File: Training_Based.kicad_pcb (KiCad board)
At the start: 2 copper layers, 210 x 140 mm, 6 parts

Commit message: update
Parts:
- added K1: FINDER-36.11, Relay_THT:Relay_SPDT_Finder_36.11, F.Cu at (191.1, 94.7)
- added K2: FINDER-36.11, Relay_THT:Relay_SPDT_Finder_36.11, F.Cu at (191.2, 76.5)
- added REF**: 7SegmentLED_LTS6760_LTS6780, Display_7Segment:7SegmentLED_LTS6760_LTS6780, F.Cu at (187.1, 45.2)
- added REF**: TerminalBlock_Altech_AK300-4_P5.00mm, TerminalBlock:TerminalBlock_Altech_AK300-4_P5.00mm, F.Cu at (218.2, 75.7)
- added REF**: 7SegmentLED_LTS6760_LTS6780, Display_7Segment:7SegmentLED_LTS6760_LTS6780, F.Cu at (200.5, 45.1)
- added REF**: ESP32-DOIT-DEVKIT, doit-esp32-devkit-kicad:ESP32-DOIT-DEVKIT, F.Cu at (126.3, 102.3)
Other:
- board text added: "ANALOG INPUT"
- board text added: "BUZZER"
- board text added: "ESP32"
- board text added: "LED OUTPUT"
- board text added: "OPTO INPUT"
- board text added: "PIR SENSOR"
- board text added: "POWER SUPPLY"
- board text added: "PROTOBOARD"
- board text added: "RELAY OUTPUT"
- board text added: "SERIAL BUS BREAKOUT AREA"
- board text added: "TEMP/HUMID"
- board text added: "ULTRASONIC SENSOR"
- board text added: "VOLUME LDR"

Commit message: update
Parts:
- removed REF** (x2): 7SegmentLED_LTS6760_LTS6780, Display_7Segment:7SegmentLED_LTS6760_LTS6780
- removed REF**: TerminalBlock_Altech_AK300-4_P5.00mm, TerminalBlock:TerminalBlock_Altech_AK300-4_P5.00mm
- removed REF**: ESP32-DOIT-DEVKIT, doit-esp32-devkit-kicad:ESP32-DOIT-DEVKIT
- added AFF1: LTS-6980HR, Display_7Segment:7SegmentLED_LTS6760_LTS6780, F.Cu at (188.2, 41.6)
- added AFF2: LTS-6980HR, Display_7Segment:7SegmentLED_LTS6760_LTS6780, F.Cu at (202.1, 41.6)
- added BZ1: Buzzer, Buzzer_Beeper:Buzzer_12x9.5RM7.6, F.Cu at (115.0, 34.6)
- added U1: HC-SR04, Library:HC-SR04, F.Cu at (63.9, 33.2)
- added U2: DHT11, Sensor:Aosong_DHT11_5.5x12.0_P2.54mm, F.Cu at (50.6, 29.6)
- moved K1 9.49 mm to (182.8, 90.0)
- moved K2 9.49 mm to (182.9, 71.8)
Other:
- board text added: "7SEGMENT LED"

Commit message: add spacerx6
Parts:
- added U3: Protoboard, Library:Protoboard, F.Cu at (126.0, 73.3)
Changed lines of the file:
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@@
     (pad "1" thru_hole circle (at 2.4 0) (size 0.8 0.8) (drill 0.5) (layers *.Cu *.Mask)
       (net 1 "GND") (pinfunction "1") (pintype "input"))
+    (model "${KIPRJMOD}/3D Model/Plastic Stick Fixed Clip On PCB.stp"
+      (offset (xyz 0 0 -14))
+      (scale (xyz 1 1 1))
+      (rotate (xyz 0 0 0))
+    )
   )
   (footprint "Relay_THT:Relay_SPDT_Finder_36.11" (layer "F.Cu")
@@
     (pad "1" thru_hole circle (at 2.4 0) (size 0.8 0.8) (drill 0.5) (layers *.Cu *.Mask)
       (net 1 "GND") (pinfunction "1") (pintype "input"))
+    (model "${KIPRJMOD}/3D Model/Plastic Stick Fixed Clip On PCB.stp"
+      (offset (xyz 0 0 -14))
+      (scale (xyz 1 1 1))
+      (rotate (xyz 0 0 0))
+    )
   )
   (footprint "MountingHole:MountingHole_3.2mm_M3_Pad_Via" (layer "F.Cu")
@@
     (pad "1" thru_hole circle (at 2.4 0) (size 0.8 0.8) (drill 0.5) (layers *.Cu *.Mask)
       (net 1 "GND") (pinfunction "1") (pintype "input"))
+    (model "${KIPRJMOD}/3D Model/Plastic Stick Fixed Clip On PCB.stp"
+      (offset (xyz 0 0 -14))
+      (scale (xyz 1 1 1))
+      (rotate (xyz 0 0 0))
+    )
   )
   (footprint "MountingHole:MountingHole_3.2mm_M3_Pad_Via" (layer "F.Cu")
@@
     (pad "1" thru_hole circle (at 2.4 0) (size 0.8 0.8) (drill 0.5) (layers *.Cu *.Mask)
       (net 1 "GND") (pinfunction "1") (pintype "input"))
+    (model "${KIPRJMOD}/3D Model/Plastic Stick Fixed Clip On PCB.stp"
+      (offset (xyz 0 0 -14))
+      (scale (xyz 1 1 1))
+      (rotate (xyz 0 0 0))
+    )
   )
   (footprint "Buzzer_Beeper:Buzzer_12x9.5RM7.6" (layer "F.Cu")
@@
     )
   )
+  (footprint "Library:Protoboard" (layer "F.Cu")
+    (at 125.95 73.3)
+    (property "Sheetfile" "Training_Based.kicad_sch")
+    (property "Sheetname" "")
+    (attr smd)
+    (fp_text reference "U3" (at 0 -0.5 unlocked) (layer "F.SilkS")
+        (effects (font (size 1 1) (thickness 0.15)))
+    )
+    (fp_text value "Protoboard" (at 0 1 unlocked) (layer "F.Fab")
+        (effects (font (size 1 1) (thickness 0.15)))
+    )
+    (fp_text user "${REFERENCE}" (at 0 2.5 unlocked) (layer "F.Fab")
+        (effects (font (size 1 1) (thickness 0.15)))
+    )
+    (fp_rect (start -41 -27) (end 41 27)
+      (stroke (width 0.12) (type default)) (fill none) (layer "F.SilkS"))
+    (model "${KIPRJMOD}/3D Model/proto_400.step"
+      (offset (xyz 0 0 0))
+      (scale (xyz 1 1 1))
+      (rotate (xyz 0 0 90))
+    )
+  )
   (footprint "Relay_THT:Relay_SPDT_Finder_36.11" (layer "F.Cu")
     (at 182.8 89.95)
@@
     (pad "1" thru_hole circle (at 2.4 0) (size 0.8 0.8) (drill 0.5) (layers *.Cu *.Mask)
       (net 1 "GND") (pinfunction "1") (pintype "input"))
+    (model "${KIPRJMOD}/3D Model/Plastic Stick Fixed Clip On PCB.stp"
+      (offset (xyz 0 0 -14))
+      (scale (xyz 1 1 1))
+      (rotate (xyz 0 0 0))
+    )
   )
   (footprint "MountingHole:MountingHole_3.2mm_M3_Pad_Via" (layer "F.Cu")
@@
     (pad "1" thru_hole circle (at 2.4 0) (size 0.8 0.8) (drill 0.5) (layers *.Cu *.Mask)
       (net 1 "GND") (pinfunction "1") (pintype "input"))
-  )
-  (gr_rect (start 226.025 113.5) (end 165.125 151.9)
+    (model "${KIPRJMOD}/3D Model/Plastic Stick Fixed Clip On PCB.stp"
+      (offset (xyz 0 0 -14))
+      (scale (xyz 1 1 1))
+      (rotate (xyz 0 0 0))
+    )
+  )
+  (gr_rect (start 175.7996 113.5) (end 226.025 151.9)
     (stroke (width 0.1) (type default)) (fill none) (layer "F.SilkS"))
   (gr_rect (start 182.95 24.025) (end 224.5 44.05)
@@
   (gr_rect (start 109.7 23.975) (end 134 44)
     (stroke (width 0.1) (type default)) (fill none) (layer "F.SilkS"))
-  (gr_rect (start 96.8 104) (end 152.05 152.3)
+  (gr_rect (start 125.15 104) (end 169.95 152.3)
     (stroke (width 0.1) (type default)) (fill none) (layer "F.SilkS"))
   (gr_rect (start 23.975 124.95) (end 71.125 151.55)
@@
     (effects (font (size 2.54 2.54) (thickness 0.2)) (justify bottom))
   )
-  (gr_text "ESP32" (at 118.481381 129.57) (layer "F.SilkS")
+  (gr_text "ESP32" (at 143.55 128.75) (layer "F.SilkS")
     (effects (font (size 2.54 2.54) (thickness 0.2) bold) (justify left bottom))
   )

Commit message: ีWork in Progress
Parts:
- removed H5, H6: MountingHole_Pad, MountingHole:MountingHole_3.2mm_M3_Pad_Via
- removed U3: Protoboard, Library:Protoboard
- added J1: Conn_01x19, Connector_PinHeader_2.54mm:PinHeader_1x19_P2.54mm_Vertical, F.Cu at (110.8, 107.2)
- added J2: Conn_01x19, Connector_PinSocket_2.54mm:PinSocket_1x19_P2.54mm_Vertical, F.Cu at (114.5, 107.2)
- added J3: Conn_01x19, Connector_PinSocket_2.54mm:PinSocket_1x19_P2.54mm_Vertical, F.Cu at (159.6, 107.2)
- added J4: Conn_01x19, Connector_PinHeader_2.54mm:PinHeader_1x19_P2.54mm_Vertical, F.Cu at (163.6, 107.2)
- added PIR1: PIR_Motion_Sensor, Sensors:PIR_HC-SR501, F.Cu at (34.2, 58.6)
- added Q1: BC817, Package_TO_SOT_SMD:SOT-23, F.Cu at (130.1, 28.9)
- added TH1: DHT11_Temperature_Humidity, Connector_PinSocket_2.54mm:PinSocket_1x03_P2.54mm_Vertical, F.Cu at (43.3, 26.3)
- U2: value DHT11 -> Protoboard; footprint Sensor:Aosong_DHT11_5.5x12.0_P2.54mm -> Library:Protoboard
- moved H2 166.2 mm to (226.0, 156.0)
- moved U2 86.1 mm to (125.0, 73.0), turned to 90 degrees
- moved BZ1 4.87 mm to (115.4, 29.8)
- moved AFF2 2.75 mm to (204.4, 40.1)
- moved AFF1 2.72 mm to (190.5, 40.1)
- moved U1 0.89 mm to (63.0, 33.0)
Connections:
- BZ1 pad 1: unconnected-(BZ1--) -> +5V
- BZ1 pad 2: unconnected-(BZ1-+) -> Net-(BZ1-+)
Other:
- board text added: "LDR"
- board text added: "VOLUME"
- board text removed: "VOLUME LDR"

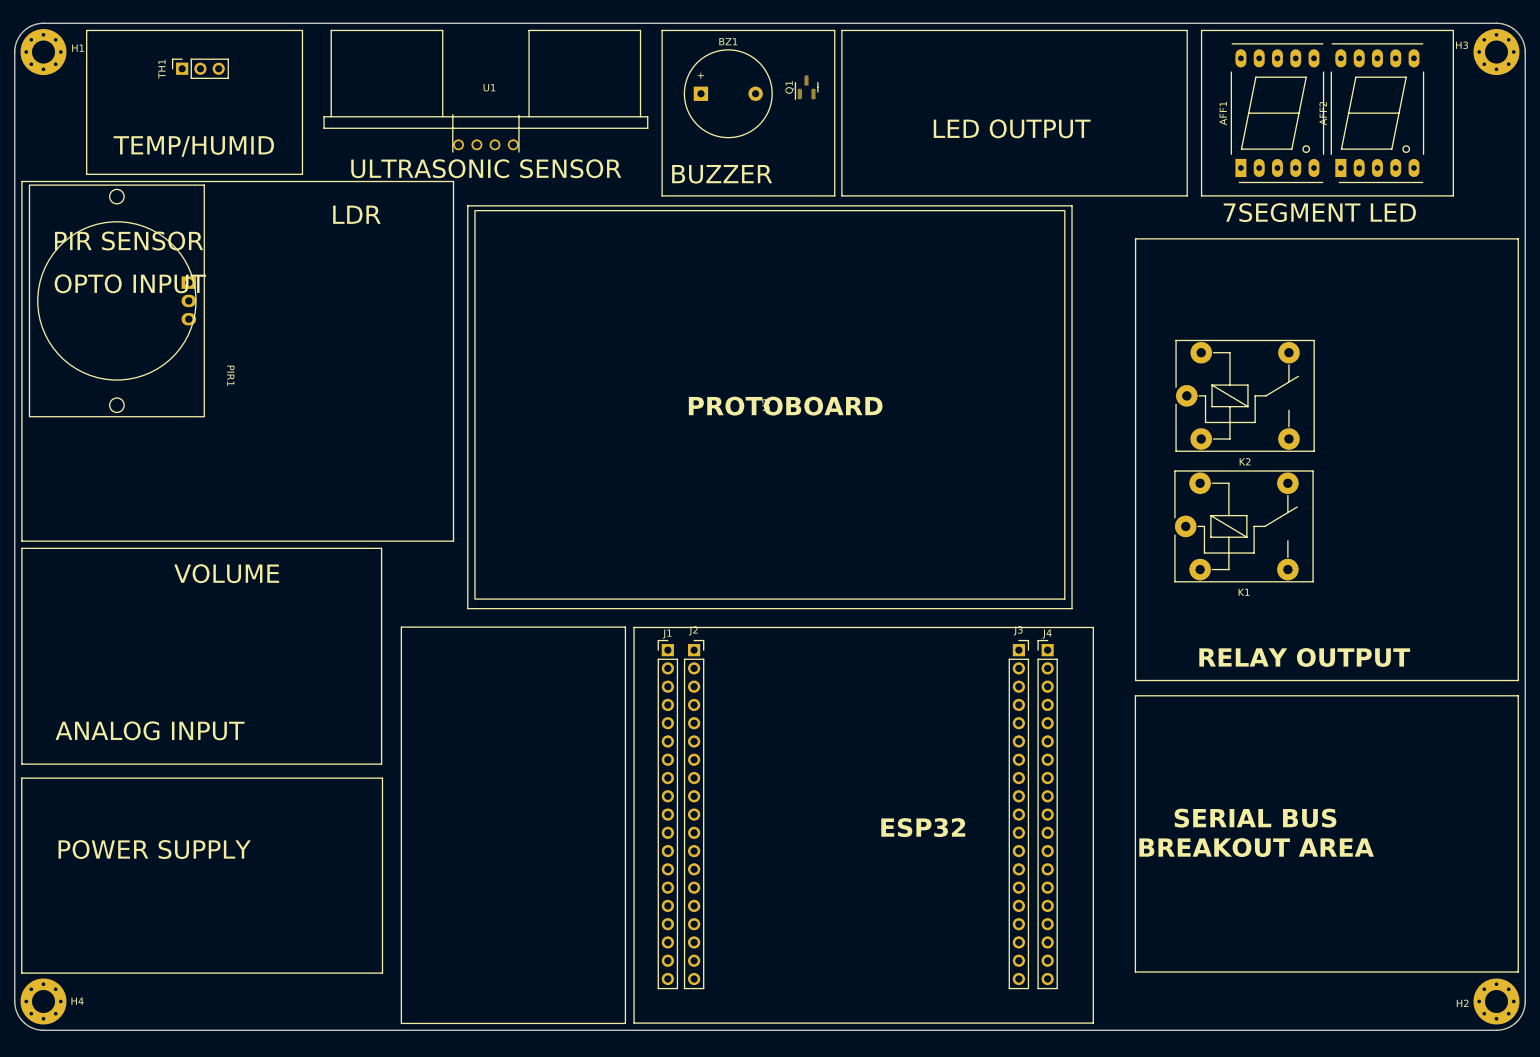
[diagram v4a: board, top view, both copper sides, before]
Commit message: add esp32 board and 3d model
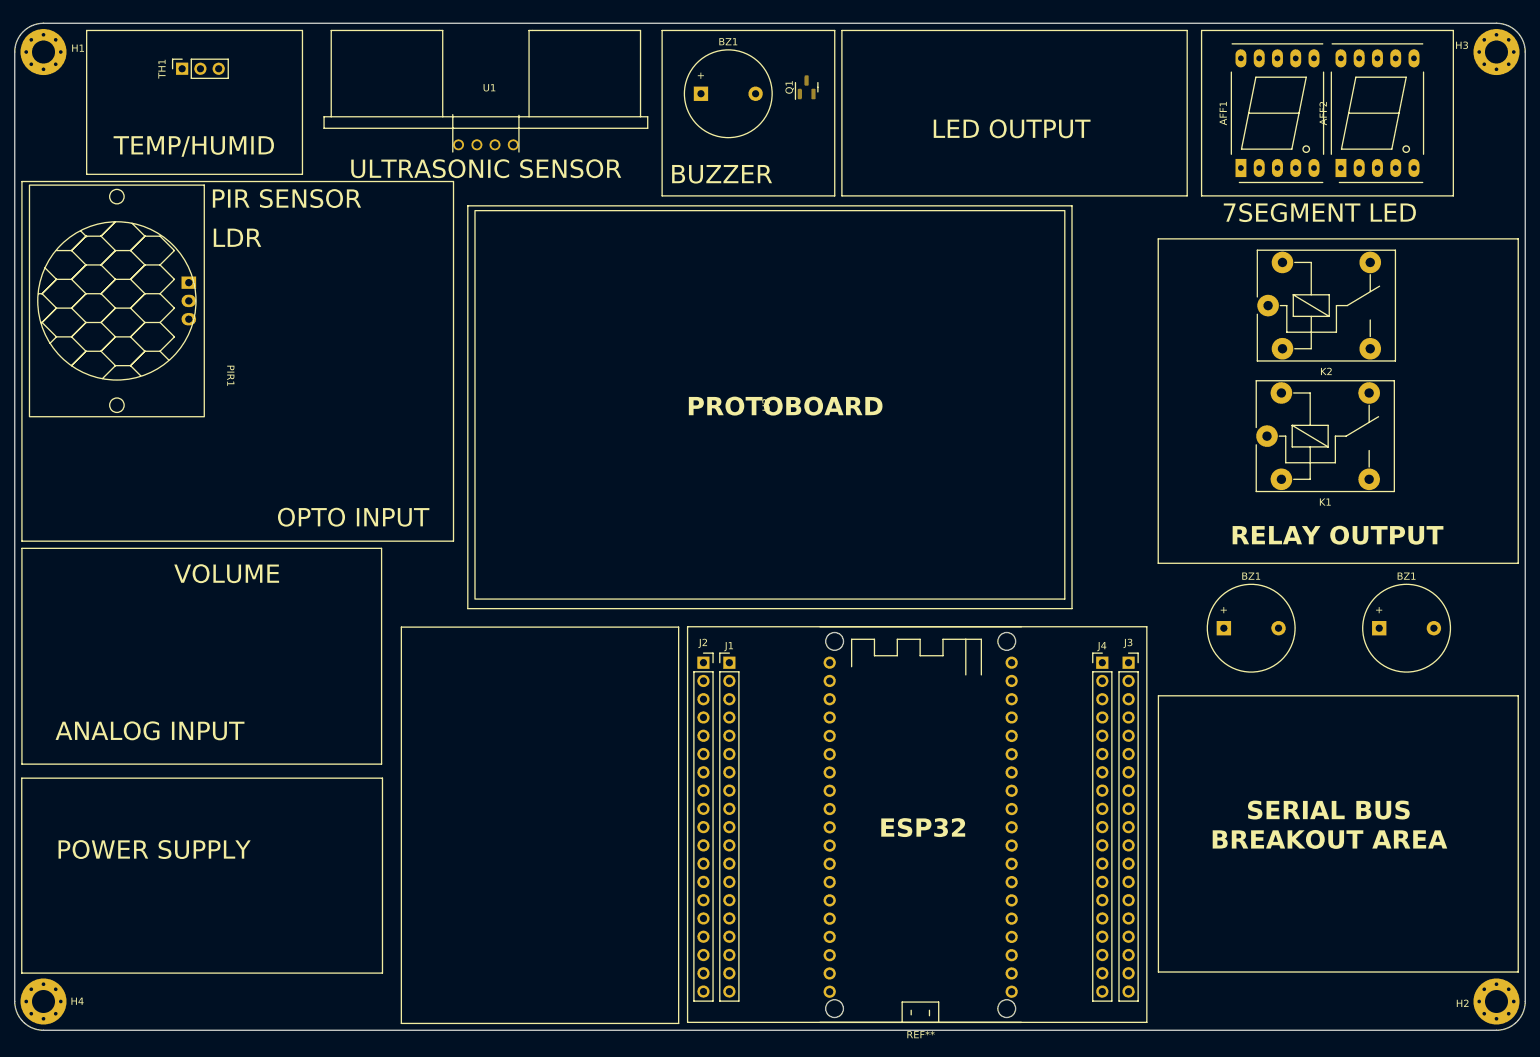
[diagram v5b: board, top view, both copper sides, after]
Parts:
- added BZ1: Buzzer, Buzzer_Beeper:Buzzer_12x9.5RM7.6, F.Cu at (188.1, 104.1)
- added BZ1: Buzzer, Buzzer_Beeper:Buzzer_12x9.5RM7.6, F.Cu at (209.7, 104.1)
- added REF**: ESP32-DevKitC, Library:ESP32-DevKitC, F.Cu at (145.9, 131.4)
- moved K2 16.9 mm to (194.2, 59.2)
- moved K1 16.9 mm to (194.1, 77.4)
- moved J3 15.3 mm to (174.8, 108.9)
- moved J1 8.73 mm to (119.3, 108.9)
- moved J4 7.80 mm to (171.2, 108.9)
- moved J2 2.18 mm to (115.8, 108.9)
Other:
- board text added: "GPIO1"

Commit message: work in progress 650723.0501
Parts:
- removed the BZ1 at (188.1, 104.1)
- removed the BZ1 at (209.7, 104.1)
- removed REF**: ESP32-DevKitC, Library:ESP32-DevKitC
- removed TH1: DHT11_Temperature_Humidity, Connector_PinSocket_2.54mm:PinSocket_1x03_P2.54mm_Vertical
- added BZ2: Buzzer, Buzzer_Beeper:Buzzer_12x9.5RM7.6, F.Cu at (131.7, 29.7)
- added J5: Conn_01x08, Connector_PinHeader_2.54mm:PinHeader_1x08_P2.54mm_Vertical, F.Cu at (156.8, 42.2)
- added LED1: LED, LED_SMD:LED_1206_3216Metric, F.Cu at (150.6, 25.4)
- added LED2: LED, LED_SMD:LED_1206_3216Metric, F.Cu at (154.9, 25.4)
- added LED3: LED, LED_SMD:LED_1206_3216Metric, F.Cu at (159.2, 25.4)
- added LED4: LED, LED_SMD:LED_1206_3216Metric, F.Cu at (163.4, 25.4)
- added LED5: LED, LED_SMD:LED_1206_3216Metric, F.Cu at (167.7, 25.4)
- added LED6: LED, LED_SMD:LED_1206_3216Metric, F.Cu at (172.0, 25.4)
- added LED7: LED, LED_SMD:LED_1206_3216Metric, F.Cu at (176.3, 25.4)
- added LED8: LED, LED_SMD:LED_1206_3216Metric, F.Cu at (180.6, 25.4)
- added Q10: BC817, Package_TO_SOT_SMD:SOT-23, F.Cu at (144.3, 34.5)
- added Q2: BC817, Package_TO_SOT_SMD:SOT-23, F.Cu at (150.6, 34.0)
- added Q3: BC817, Package_TO_SOT_SMD:SOT-23, F.Cu at (154.9, 34.0)
- added Q4: BC817, Package_TO_SOT_SMD:SOT-23, F.Cu at (159.2, 34.0)
- added Q5: BC817, Package_TO_SOT_SMD:SOT-23, F.Cu at (163.4, 34.0)
- added Q6: BC817, Package_TO_SOT_SMD:SOT-23, F.Cu at (167.7, 34.0)
- added Q7: BC817, Package_TO_SOT_SMD:SOT-23, F.Cu at (172.0, 34.0)
- added Q8: BC817, Package_TO_SOT_SMD:SOT-23, F.Cu at (176.3, 34.0)
- added Q9: BC817, Package_TO_SOT_SMD:SOT-23, F.Cu at (180.6, 34.0)
- added R1: R_Small, Resistor_SMD:R_0603_1608Metric, F.Cu at (150.6, 29.9)
- added R10: R_Small, Resistor_SMD:R_0603_1608Metric, F.Cu at (167.7, 29.9)
- added R11: R_Small, Resistor_SMD:R_0603_1608Metric, F.Cu at (171.8, 37.0)
- added R12: R_Small, Resistor_SMD:R_0603_1608Metric, F.Cu at (172.0, 29.9)
- added R13: R_Small, Resistor_SMD:R_0603_1608Metric, F.Cu at (175.7, 37.1)
- added R14: R_Small, Resistor_SMD:R_0603_1608Metric, F.Cu at (176.3, 29.9)
- added R15: R_Small, Resistor_SMD:R_0603_1608Metric, F.Cu at (180.3, 37.1)
- added R16: R_Small, Resistor_SMD:R_0603_1608Metric, F.Cu at (180.6, 29.9)
- added R17: R_Small, Resistor_SMD:R_0603_1608Metric, F.Cu at (143.3, 39.0)
- added R18: R_Small, Resistor_SMD:R_0603_1608Metric, F.Cu at (125.2, 39.0)
- added R2: R_Small, Resistor_SMD:R_0603_1608Metric, F.Cu at (150.6, 37.0)
- added R3: R_Small, Resistor_SMD:R_0603_1608Metric, F.Cu at (154.9, 37.0)
- added R4: R_Small, Resistor_SMD:R_0603_1608Metric, F.Cu at (154.9, 29.9)
- added R5: R_Small, Resistor_SMD:R_0603_1608Metric, F.Cu at (159.2, 37.1)
- added R6: R_Small, Resistor_SMD:R_0603_1608Metric, F.Cu at (159.2, 29.9)
- added R7: R_Small, Resistor_SMD:R_0603_1608Metric, F.Cu at (163.6, 37.1)
- added R8: R_Small, Resistor_SMD:R_0603_1608Metric, F.Cu at (163.4, 29.9)
- added R9: R_Small, Resistor_SMD:R_0603_1608Metric, F.Cu at (167.7, 37.1)
- added TH2: DHT22_Temperature_Humidity, Connector_PinSocket_2.54mm:PinSocket_1x04_P2.54mm_Vertical, F.Cu at (48.2, 24.6)
- added U3: esp32_38_pins-custom_library, Library:ESP32-DevKitC, F.Cu at (145.5, 131.4)
- moved Q1 6.81 mm to (126.2, 34.5)
- moved BZ1 1.55 mm to (113.8, 29.7)
- moved J3 0.40 mm to (175.2, 108.9)
- moved J4 0.40 mm to (171.6, 108.9)
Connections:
- net Net-(J1-Pin_1) renamed +3.3V
- net Net-(J1-Pin_10) renamed /GPIO26
- net Net-(J1-Pin_11) renamed /GPIO27
- net Net-(J1-Pin_12) renamed /GPIO14
- net Net-(J1-Pin_13) renamed /GPIO12
- net Net-(J1-Pin_15) renamed /GPIO13
- net Net-(J1-Pin_16) renamed /GPIO9
- net Net-(J1-Pin_17) renamed /GPIO10
- net Net-(J1-Pin_18) renamed /GPIO11
- net Net-(J1-Pin_2) renamed /EN_RST
- net Net-(J1-Pin_3) renamed /GPI36
- net Net-(J1-Pin_4) renamed /GPI39
- net Net-(J1-Pin_5) renamed /GPI34
- net Net-(J1-Pin_6) renamed /GPI35
- net Net-(J1-Pin_7) renamed /GPIO32
- net Net-(J1-Pin_8) renamed /GPIO33
- net Net-(J1-Pin_9) renamed /GPIO25
- net Net-(J3-Pin_10) renamed /GPIO5
- net Net-(J3-Pin_11) renamed /GPIO17
- net Net-(J3-Pin_12) renamed /GPIO16
- net Net-(J3-Pin_13) renamed /GPIO4
- net Net-(J3-Pin_14) renamed /GPIO0
- net Net-(J3-Pin_15) renamed /GPIO2
- net Net-(J3-Pin_16) renamed /GPIO15
- net Net-(J3-Pin_17) renamed /GPIO8
- net Net-(J3-Pin_18) renamed /GPIO7
- net Net-(J3-Pin_19) renamed /GPIO6
- net Net-(J3-Pin_2) renamed /GPIO23
- net Net-(J3-Pin_3) renamed /GPIO22
- net Net-(J3-Pin_4) renamed /GPIO1
- net Net-(J3-Pin_5) renamed /GPIO3
- net Net-(J3-Pin_6) renamed /GPIO21
- net Net-(J3-Pin_8) renamed /GPIO19
- net Net-(J3-Pin_9) renamed /GPIO18
- J1 pad 14: Net-(J1-Pin_14) -> GND
- J1 pad 19: Net-(J1-Pin_19) -> +5V
- J2 pad 14: Net-(J1-Pin_14) -> GND
- J2 pad 19: Net-(J1-Pin_19) -> +5V
- J3 pad 1: Net-(J3-Pin_1) -> GND
- J3 pad 7: Net-(J3-Pin_7) -> GND
- J4 pad 1: Net-(J3-Pin_1) -> GND
- J4 pad 7: Net-(J3-Pin_7) -> GND
- Q1 pad 1: unconnected-(Q1-B) -> Net-(R18-Pad2)
- U1 pad 1: (no net) -> unconnected-(U1-Vcc)
- U1 pad 2: (no net) -> unconnected-(U1-Trig)
- U1 pad 3: (no net) -> unconnected-(U1-Echo)
- U1 pad 4: (no net) -> unconnected-(U1-Gnd)
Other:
- board text added: "+5V"
- board text added: "1"
- board text added: "2"
- board text added: "3"
- board text added: "4"
- board text added: "5"
- board text added: "6"
- board text added: "7"
- board text added: "8"
- board text added: "EN-RST"
- board text added: "GND"
- board text added: "GPI34"
- board text added: "GPI35"
- board text added: "GPI36"
- board text added: "GPI39"
- board text added: "GPIO0"
- board text added: "GPIO10"
- board text added: "GPIO11"
- board text added: "GPIO12"
- board text added: "GPIO13"
- board text added: "GPIO14"
- board text added: "GPIO15"
- board text added: "GPIO16"
- board text added: "GPIO17"
- board text added: "GPIO18"
- board text added: "GPIO19"
- board text added: "GPIO2"
- board text added: "GPIO21"
- board text added: "GPIO22"
- board text added: "GPIO23"
- board text added: "GPIO25"
- board text added: "GPIO26"
- board text added: "GPIO27"
- board text added: "GPIO3"
- board text added: "GPIO32"
- board text added: "GPIO33"
- board text added: "GPIO4"
- board text added: "GPIO5"
- board text added: "GPIO6"
- board text added: "GPIO7"
- board text added: "GPIO8"
- board text added: "GPIO9"
- board text added: "LED"
- board text removed: "LED OUTPUT"

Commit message: WIP 6507230502
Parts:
- added Q11: BC817, Package_TO_SOT_SMD:SOT-23, F.Cu at (189.0, 72.2)
- added Q12: BC817, Package_TO_SOT_SMD:SOT-23, F.Cu at (187.8, 53.5)
- added R19: R_Small, Resistor_SMD:R_0603_1608Metric, F.Cu at (186.1, 72.2)
- added R20: R_Small, Resistor_SMD:R_0603_1608Metric, F.Cu at (185.1, 53.4)
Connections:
- K1 pad A1: unconnected-(K1-PadA1) -> +5V
- K1 pad A2: unconnected-(K1-PadA2) -> Net-(Q11-C)
- K2 pad A1: unconnected-(K2-PadA1) -> +5V
- K2 pad A2: unconnected-(K2-PadA2) -> Net-(D2-A)

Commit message: Update Training_Based.kicad_pcb
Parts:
- added J6: Conn_02x02_Row_Letter_Last, Connector_PinSocket_2.54mm:PinSocket_2x02_P2.54mm_Vertical, F.Cu at (43.1, 36.5)
- added J7: Conn_02x02_Row_Letter_Last, Connector_PinSocket_2.54mm:PinSocket_2x02_P2.54mm_Vertical, F.Cu at (94.6, 40.8)
- added J8: Conn_02x02_Row_Letter_Last, Connector_PinSocket_2.54mm:PinSocket_2x02_P2.54mm_Vertical, F.Cu at (132.4, 41.1)
- moved K1 7.92 mm to (194.1, 85.3)
- moved K2 7.92 mm to (194.2, 67.2)
- moved Q11 7.92 mm to (189.0, 80.1)
- moved Q12 7.92 mm to (187.8, 61.4)
- moved R19 7.92 mm to (186.1, 80.1)
- moved R20 7.92 mm to (185.1, 61.3)
- moved TH2 3.53 mm to (48.8, 28.1)
- moved R17 1.84 mm to (142.9, 37.1), turned to 0 degrees
- moved R18 1.84 mm to (124.8, 37.1), turned to 180 degrees
- moved BZ1 1.72 mm to (114.1, 28.0)
- moved BZ2 1.72 mm to (131.9, 28.0)
- moved Q10 1.37 mm to (142.9, 34.2)
- moved Q1 1.37 mm to (124.8, 34.2)
- moved AFF1 0.98 mm to (190.2, 39.2)
- moved AFF2 0.98 mm to (204.1, 39.2)
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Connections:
- TH2 pad 1: unconnected-(TH2-VDD) -> +5V
- TH2 pad 2: unconnected-(TH2-DATA) -> /DATA
- TH2 pad 4: unconnected-(TH2-GND) -> GND
- U1 pad 1: unconnected-(U1-Vcc) -> +5V
- U1 pad 2: unconnected-(U1-Trig) -> /Trig
- U1 pad 3: unconnected-(U1-Echo) -> /Echo
- U1 pad 4: unconnected-(U1-Gnd) -> GND
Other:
- board text added: "BZ1"
- board text added: "BZ2"
- board text added: "DATA"
- board text added: "Echo"
- board text added: "Trig"
- board text added: "X"
